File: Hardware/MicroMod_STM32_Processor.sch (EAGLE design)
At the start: 36 parts, among them J1 MICROMOD-2222, Q1 MOSFET_PCH-DMG2305UX-7, U1 STM32F405RGT6, U3 W25QXX128MBIT-6X5, Y1 12MHz, Y2 32.768kHz

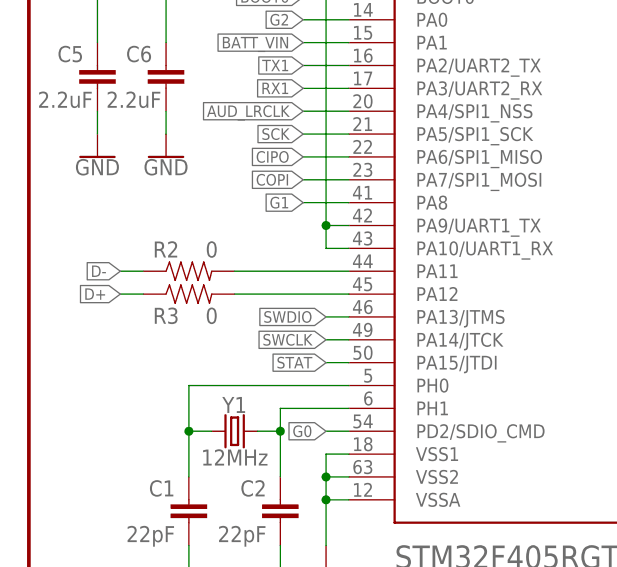
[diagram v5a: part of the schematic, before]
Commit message: Updated USB Load resistors
Replaced 0 ohm resistors with 22 ohm
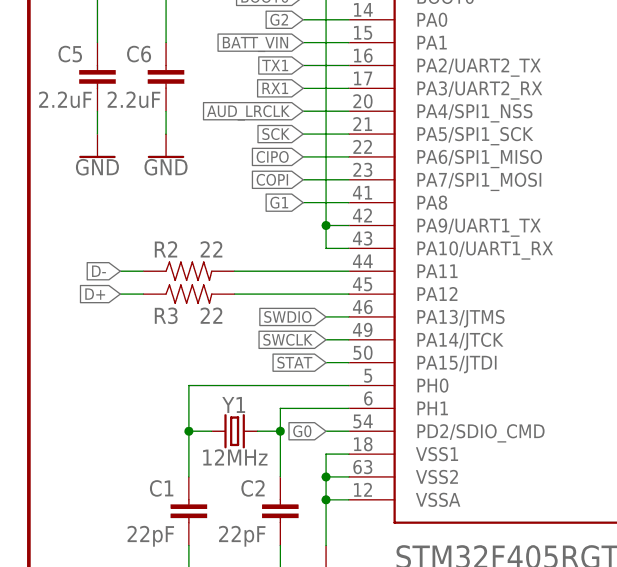
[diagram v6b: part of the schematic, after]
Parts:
- R2, R3: value 0 -> 22; device SparkFun-Resistors:0OHM-0402T-1/10W -> SparkFun-Resistors:22OHM-0402T-1/16W-1%
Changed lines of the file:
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@@
 <?xml version="1.0" encoding="utf-8"?>
 <!DOCTYPE eagle SYSTEM "eagle.dtd">
-<eagle version="9.5.2">
+<eagle version="9.6.2">
 <drawing>
 <settings>
@@
 <part name="R12" library="SparkFun-Resistors" deviceset="1KOHM" device="-0402T-1/16W-1%" value="1k"/>
 <part name="GND35" library="SparkFun-PowerSymbols" deviceset="GND" device=""/>
-<part name="R2" library="SparkFun-Resistors" deviceset="0OHM" device="-0402T-1/10W" value="0"/>
-<part name="R3" library="SparkFun-Resistors" deviceset="0OHM" device="-0402T-1/10W" value="0"/>
+<part name="R2" library="SparkFun-Resistors" deviceset="22OHM" device="-0402T-1/16W-1%" value="22"/>
+<part name="R3" library="SparkFun-Resistors" deviceset="22OHM" device="-0402T-1/16W-1%" value="22"/>
 <part name="R4" library="SparkFun-Resistors" deviceset="5.1KOHM" device="-0402T-1/16W-1%" value="5.1k"/>
 <part name="C15" library="SparkFun-Capacitors" deviceset="0.1UF" device="-0402T-10V-10%-X7R" value="0.1uF"/>

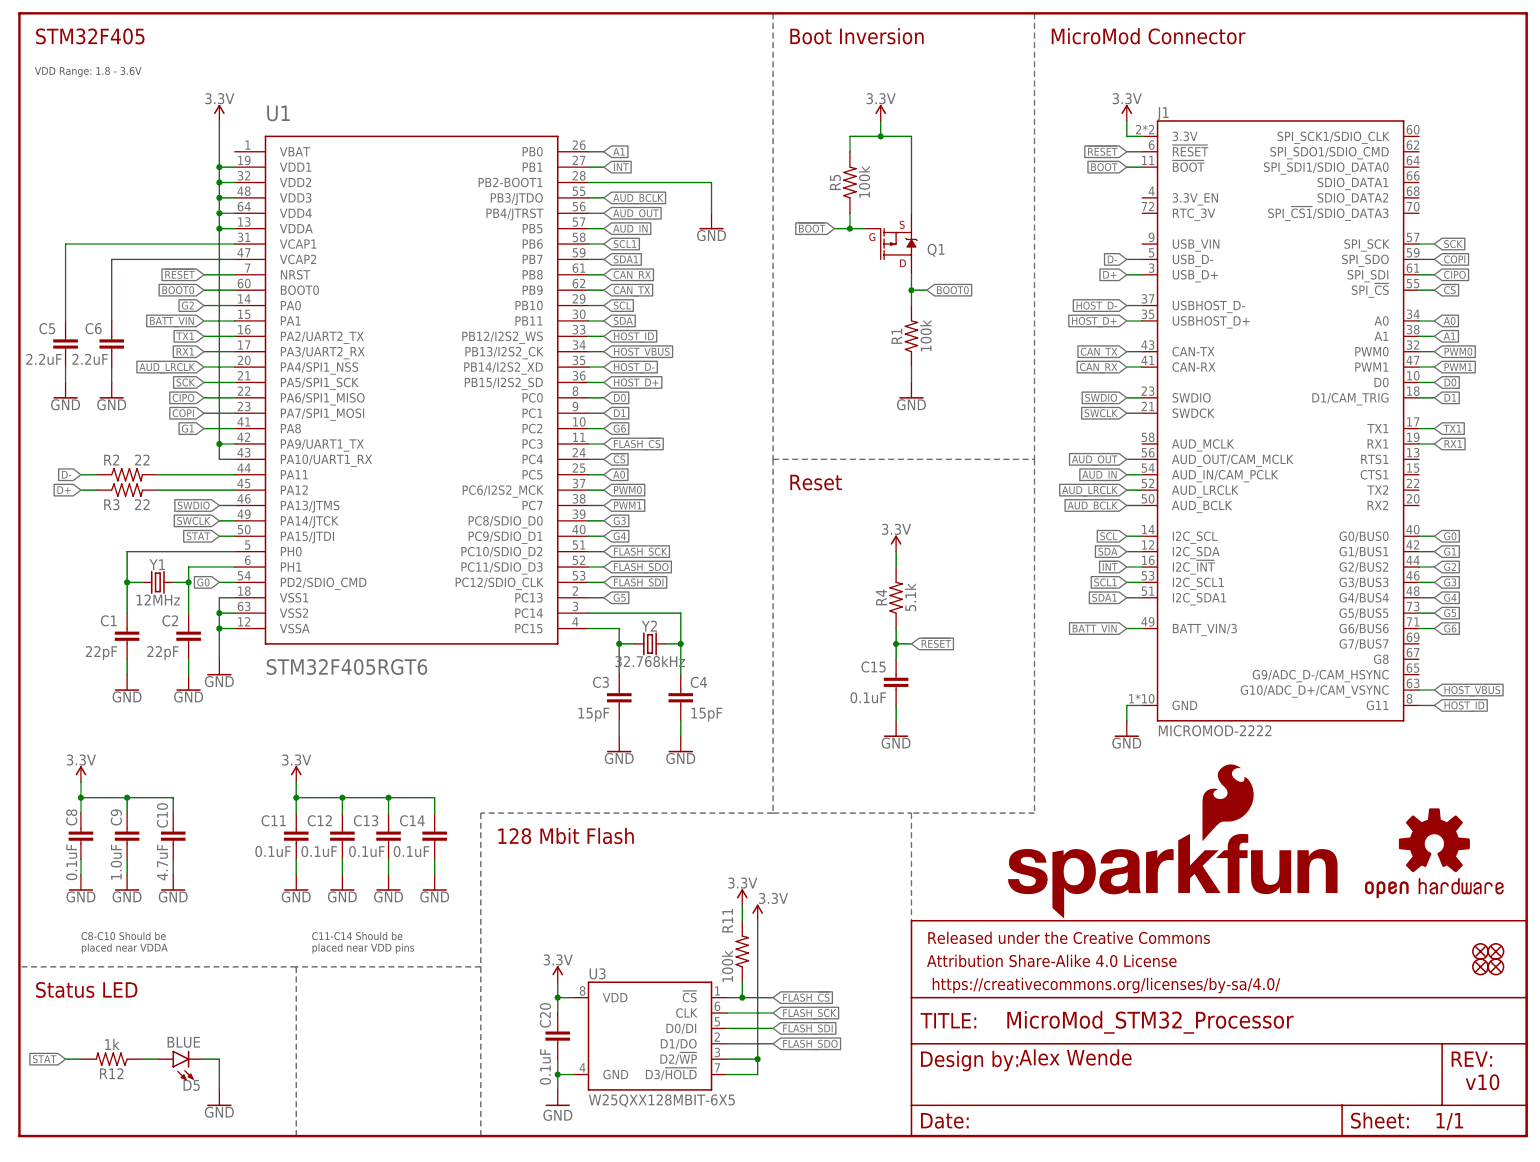
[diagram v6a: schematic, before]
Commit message: Swap USART2 for USART1, connect USART2 to ground.
Also renamed COPI/CIPO to POCI/PICO to match new naming conventions.
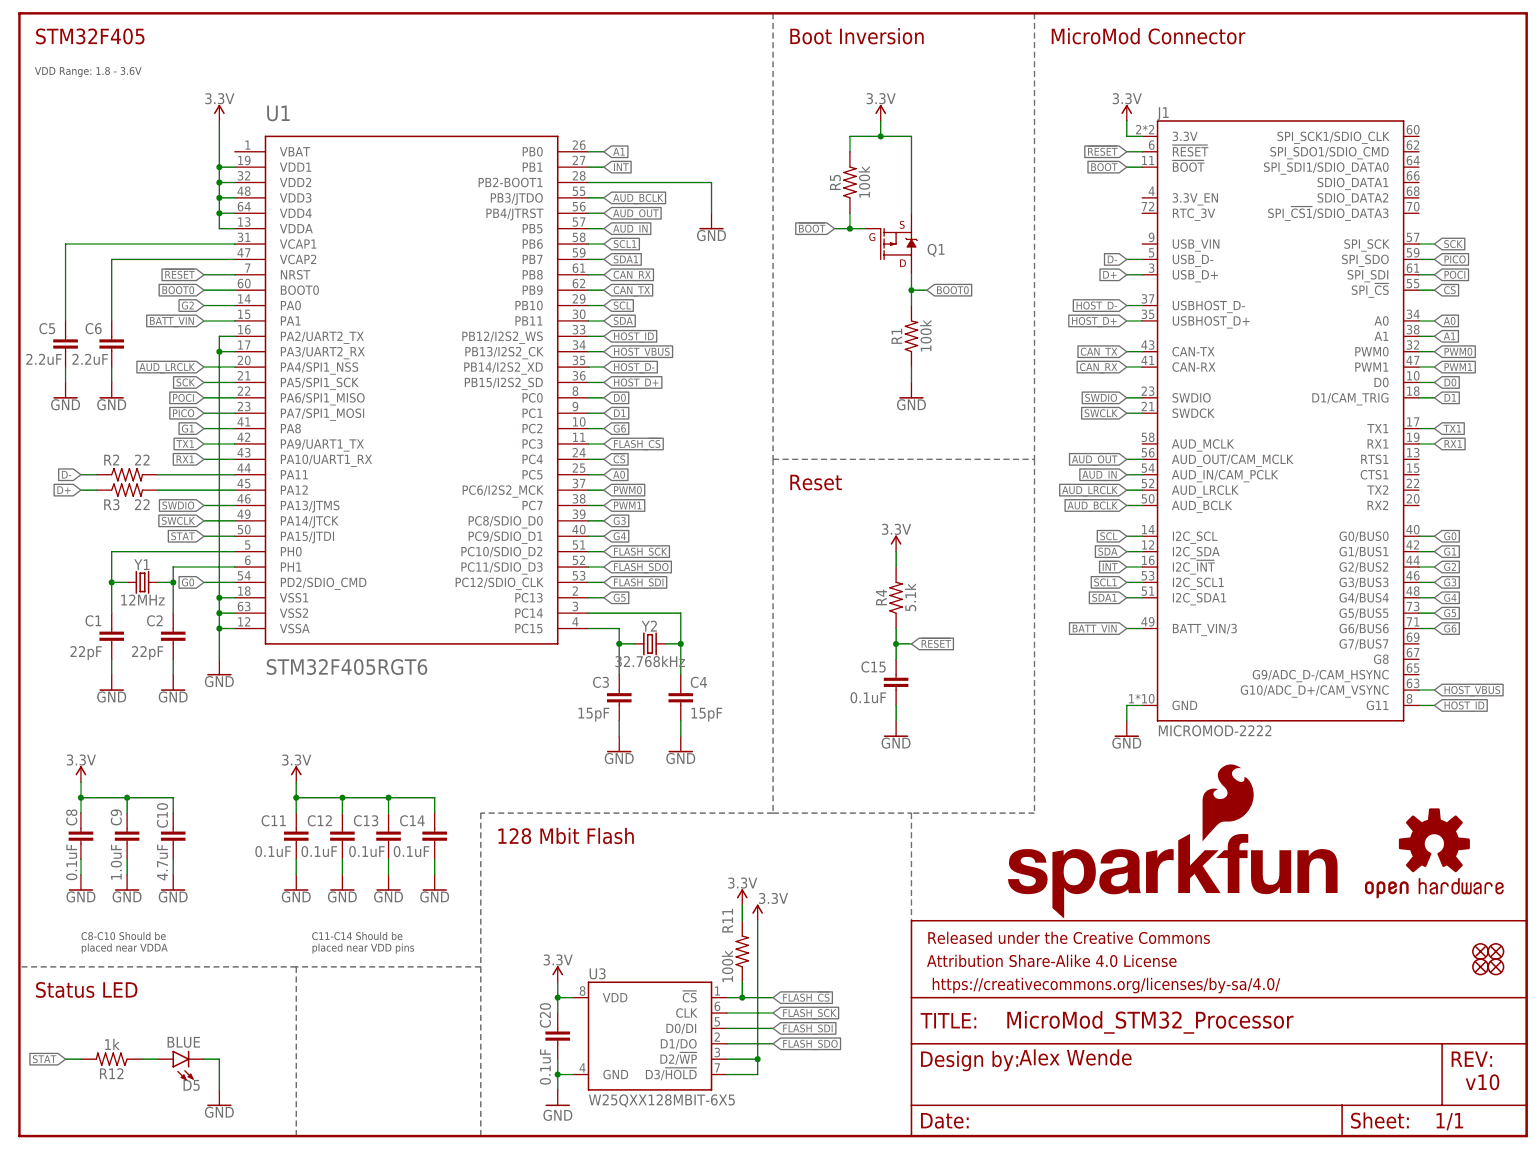
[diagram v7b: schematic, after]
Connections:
- net CIPO renamed POCI
- net COPI renamed PICO
- net 3.3V: no longer U1.PA10/UART1_RX, U1.PA9/UART1_TX
- net GND: now also U1.PA2/UART2_TX, U1.PA3/UART2_RX
- net RX1: now also U1.PA10/UART1_RX; no longer U1.PA3/UART2_RX
- net TX1: now also U1.PA9/UART1_TX; no longer U1.PA2/UART2_TX
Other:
- moved on the sheet: C1, C2, Y1
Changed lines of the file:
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@@
 <drawing>
 <settings>
-<setting alwaysvectorfont="yes"/>
+<setting alwaysvectorfont="no"/>
 <setting verticaltext="up"/>
 </settings>
@@
 <attribute name="VALUE" x="40.64" y="76.2" size="2.54" layer="96" font="vector"/>
 </instance>
-<instance part="Y1" gate="G$1" x="22.86" y="91.44" smashed="yes">
-<attribute name="NAME" x="22.86" y="93.472" size="1.778" layer="95" font="vector" align="bottom-center"/>
-<attribute name="VALUE" x="22.86" y="89.408" size="1.778" layer="96" font="vector" align="top-center"/>
+<instance part="Y1" gate="G$1" x="20.32" y="91.44" smashed="yes">
+<attribute name="NAME" x="20.32" y="93.472" size="1.778" layer="95" font="vector" align="bottom-center"/>
+<attribute name="VALUE" x="20.32" y="89.408" size="1.778" layer="96" font="vector" align="top-center"/>
 </instance>
 <instance part="Y2" gate="G$1" x="104.14" y="81.28" smashed="yes">
@@
 <attribute name="VALUE" x="104.14" y="79.248" size="1.778" layer="96" font="vector" align="top-center"/>
 </instance>
-<instance part="C1" gate="G$1" x="17.78" y="81.28" smashed="yes" rot="MR0">
-<attribute name="NAME" x="16.256" y="84.201" size="1.778" layer="95" font="vector" rot="MR0"/>
-<attribute name="VALUE" x="16.256" y="79.121" size="1.778" layer="96" font="vector" rot="MR0"/>
-</instance>
-<instance part="C2" gate="G$1" x="27.94" y="81.28" smashed="yes" rot="MR0">
-<attribute name="NAME" x="26.416" y="84.201" size="1.778" layer="95" font="vector" rot="MR0"/>
-<attribute name="VALUE" x="26.416" y="79.121" size="1.778" layer="96" font="vector" rot="MR0"/>
+<instance part="C1" gate="G$1" x="15.24" y="81.28" smashed="yes" rot="MR0">
+<attribute name="NAME" x="13.716" y="84.201" size="1.778" layer="95" font="vector" rot="MR0"/>
+<attribute name="VALUE" x="13.716" y="79.121" size="1.778" layer="96" font="vector" rot="MR0"/>
+</instance>
+<instance part="C2" gate="G$1" x="25.4" y="81.28" smashed="yes" rot="MR0">
+<attribute name="NAME" x="23.876" y="84.201" size="1.778" layer="95" font="vector" rot="MR0"/>
+<attribute name="VALUE" x="23.876" y="79.121" size="1.778" layer="96" font="vector" rot="MR0"/>
 </instance>
 <instance part="C3" gate="G$1" x="99.06" y="71.12" smashed="yes" rot="MR0">
@@
 <attribute name="VALUE" x="33.02" y="75.946" size="1.778" layer="96" font="vector" align="top-center"/>
 </instance>
-<instance part="GND6" gate="1" x="27.94" y="73.66" smashed="yes">
-<attribute name="VALUE" x="27.94" y="73.406" size="1.778" layer="96" font="vector" align="top-center"/>
-</instance>
-<instance part="GND10" gate="1" x="17.78" y="73.66" smashed="yes">
-<attribute name="VALUE" x="17.78" y="73.406" size="1.778" layer="96" font="vector" align="top-center"/>
+<instance part="GND6" gate="1" x="25.4" y="73.66" smashed="yes">
+<attribute name="VALUE" x="25.4" y="73.406" size="1.778" layer="96" font="vector" align="top-center"/>
+</instance>
+<instance part="GND10" gate="1" x="15.24" y="73.66" smashed="yes">
+<attribute name="VALUE" x="15.24" y="73.406" size="1.778" layer="96" font="vector" align="top-center"/>
 </instance>
 <instance part="GND11" gate="1" x="109.22" y="63.5" smashed="yes">
@@
 <pinref part="Y1" gate="G$1" pin="2"/>
 <pinref part="C2" gate="G$1" pin="1"/>
-<wire x1="25.4" y1="91.44" x2="27.94" y2="91.44" width="0.1524" layer="91"/>
-<wire x1="27.94" y1="91.44" x2="27.94" y2="86.36" width="0.1524" layer="91"/>
+<wire x1="22.86" y1="91.44" x2="25.4" y2="91.44" width="0.1524" layer="91"/>
+<wire x1="25.4" y1="91.44" x2="25.4" y2="86.36" width="0.1524" layer="91"/>
 <pinref part="U1" gate="G$1" pin="PH1"/>
-<wire x1="35.56" y1="93.98" x2="27.94" y2="93.98" width="0.1524" layer="91"/>
-<wire x1="27.94" y1="93.98" x2="27.94" y2="91.44" width="0.1524" layer="91"/>
-<junction x="27.94" y="91.44"/>
+<wire x1="35.56" y1="93.98" x2="25.4" y2="93.98" width="0.1524" layer="91"/>
+<wire x1="25.4" y1="93.98" x2="25.4" y2="91.44" width="0.1524" layer="91"/>
+<junction x="25.4" y="91.44"/>
 </segment>
 </net>
@@
 <pinref part="Y1" gate="G$1" pin="1"/>
 <pinref part="C1" gate="G$1" pin="1"/>
-<wire x1="20.32" y1="91.44" x2="17.78" y2="91.44" width="0.1524" layer="91"/>
-<wire x1="17.78" y1="91.44" x2="17.78" y2="86.36" width="0.1524" layer="91"/>
+<wire x1="17.78" y1="91.44" x2="15.24" y2="91.44" width="0.1524" layer="91"/>
+<wire x1="15.24" y1="91.44" x2="15.24" y2="86.36" width="0.1524" layer="91"/>
 <pinref part="U1" gate="G$1" pin="PH0"/>
-<wire x1="35.56" y1="96.52" x2="17.78" y2="96.52" width="0.1524" layer="91"/>
-<wire x1="17.78" y1="96.52" x2="17.78" y2="91.44" width="0.1524" layer="91"/>
-<junction x="17.78" y="91.44"/>
+<wire x1="35.56" y1="96.52" x2="15.24" y2="96.52" width="0.1524" layer="91"/>
+<wire x1="15.24" y1="96.52" x2="15.24" y2="91.44" width="0.1524" layer="91"/>
+<junction x="15.24" y="91.44"/>
 </segment>
 </net>
@@
 <segment>
 <pinref part="U1" gate="G$1" pin="PA13/JTMS"/>
-<wire x1="35.56" y1="104.14" x2="33.02" y2="104.14" width="0.1524" layer="91"/>
-<label x="33.02" y="104.14" size="1.27" layer="95" font="vector" rot="R180" xref="yes"/>
+<wire x1="35.56" y1="104.14" x2="30.48" y2="104.14" width="0.1524" layer="91"/>
+<label x="30.48" y="104.14" size="1.27" layer="95" font="vector" rot="R180" xref="yes"/>
 </segment>
 <segment>
@@
 <segment>
 <pinref part="U1" gate="G$1" pin="PA14/JTCK"/>
-<wire x1="35.56" y1="101.6" x2="33.02" y2="101.6" width="0.1524" layer="91"/>
-<label x="33.02" y="101.6" size="1.27" layer="95" font="vector" rot="R180" xref="yes"/>
+<wire x1="35.56" y1="101.6" x2="30.48" y2="101.6" width="0.1524" layer="91"/>
+<label x="30.48" y="101.6" size="1.27" layer="95" font="vector" rot="R180" xref="yes"/>
 </segment>
 <segment>
@@
 </segment>
 </net>
-<net name="CIPO" class="0">
+<net name="POCI" class="0">
 <segment>
 <pinref part="U1" gate="G$1" pin="PA6/SPI1_MISO"/>
@@
 </segment>
 </net>
-<net name="COPI" class="0">
+<net name="PICO" class="0">
 <segment>
 <pinref part="U1" gate="G$1" pin="PA7/SPI1_MOSI"/>
@@
 </segment>
 <segment>
-<pinref part="U1" gate="G$1" pin="PA2/UART2_TX"/>
-<wire x1="35.56" y1="132.08" x2="30.48" y2="132.08" width="0.1524" layer="91"/>
-<label x="30.48" y="132.08" size="1.27" layer="95" font="vector" rot="R180" xref="yes"/>
+<wire x1="35.56" y1="114.3" x2="30.48" y2="114.3" width="0.1524" layer="91"/>
+<label x="30.48" y="114.3" size="1.27" layer="95" font="vector" rot="R180" xref="yes"/>
+<pinref part="U1" gate="G$1" pin="PA9/UART1_TX"/>
 </segment>
 </net>
@@
 </segment>
 <segment>
-<pinref part="U1" gate="G$1" pin="PA3/UART2_RX"/>
-<wire x1="35.56" y1="129.54" x2="30.48" y2="129.54" width="0.1524" layer="91"/>
-<label x="30.48" y="129.54" size="1.27" layer="95" font="vector" rot="R180" xref="yes"/>
+<wire x1="35.56" y1="111.76" x2="30.48" y2="111.76" width="0.1524" layer="91"/>
+<label x="30.48" y="111.76" size="1.27" layer="95" font="vector" rot="R180" xref="yes"/>
+<pinref part="U1" gate="G$1" pin="PA10/UART1_RX"/>
 </segment>
 </net>
@@
 <segment>
 <pinref part="U1" gate="G$1" pin="PD2/SDIO_CMD"/>
-<wire x1="35.56" y1="91.44" x2="33.02" y2="91.44" width="0.1524" layer="91"/>
-<label x="33.02" y="91.44" size="1.27" layer="95" rot="R180" xref="yes"/>
+<wire x1="35.56" y1="91.44" x2="30.48" y2="91.44" width="0.1524" layer="91"/>
+<label x="30.48" y="91.44" size="1.27" layer="95" rot="R180" xref="yes"/>
 </segment>
 </net>
@@
 <segment>
 <pinref part="U1" gate="G$1" pin="PA15/JTDI"/>
-<wire x1="33.02" y1="99.06" x2="35.56" y2="99.06" width="0.1524" layer="91"/>
-<label x="33.02" y="99.06" size="1.27" layer="95" rot="R180" xref="yes"/>
+<wire x1="30.48" y1="99.06" x2="35.56" y2="99.06" width="0.1524" layer="91"/>
+<label x="30.48" y="99.06" size="1.27" layer="95" rot="R180" xref="yes"/>
 </segment>
 </net>
@@
 <junction x="33.02" y="83.82"/>
 <pinref part="GND4" gate="1" pin="GND"/>
+<pinref part="U1" gate="G$1" pin="PA2/UART2_TX"/>
+<wire x1="35.56" y1="132.08" x2="33.02" y2="132.08" width="0.1524" layer="91"/>
+<wire x1="33.02" y1="132.08" x2="33.02" y2="129.54" width="0.1524" layer="91"/>
+<junction x="33.02" y="88.9"/>
+<pinref part="U1" gate="G$1" pin="PA3/UART2_RX"/>
+<wire x1="33.02" y1="129.54" x2="33.02" y2="88.9" width="0.1524" layer="91"/>
+<wire x1="35.56" y1="129.54" x2="33.02" y2="129.54" width="0.1524" layer="91"/>
+<junction x="33.02" y="129.54"/>
 </segment>
 <segment>
 <pinref part="C2" gate="G$1" pin="2"/>
-<wire x1="27.94" y1="78.74" x2="27.94" y2="76.2" width="0.1524" layer="91"/>
+<wire x1="25.4" y1="78.74" x2="25.4" y2="76.2" width="0.1524" layer="91"/>
 <pinref part="GND6" gate="1" pin="GND"/>
 </segment>
 <segment>
 <pinref part="C1" gate="G$1" pin="2"/>
-<wire x1="17.78" y1="78.74" x2="17.78" y2="76.2" width="0.1524" layer="91"/>
+<wire x1="15.24" y1="78.74" x2="15.24" y2="76.2" width="0.1524" layer="91"/>
 <pinref part="GND10" gate="1" pin="GND"/>
 </segment>
@@
 </segment>
 <segment>
-<pinref part="U1" gate="G$1" pin="PA10/UART1_RX"/>
-<wire x1="35.56" y1="111.76" x2="33.02" y2="111.76" width="0.1524" layer="91"/>
-<wire x1="33.02" y1="111.76" x2="33.02" y2="114.3" width="0.1524" layer="91"/>
-<pinref part="U1" gate="G$1" pin="PA9/UART1_TX"/>
-<wire x1="33.02" y1="114.3" x2="33.02" y2="149.86" width="0.1524" layer="91"/>
 <wire x1="33.02" y1="149.86" x2="33.02" y2="152.4" width="0.1524" layer="91"/>
 <wire x1="33.02" y1="152.4" x2="33.02" y2="154.94" width="0.1524" layer="91"/>
@@
 <wire x1="33.02" y1="157.48" x2="33.02" y2="160.02" width="0.1524" layer="91"/>
 <wire x1="33.02" y1="160.02" x2="33.02" y2="167.64" width="0.1524" layer="91"/>
-<wire x1="35.56" y1="114.3" x2="33.02" y2="114.3" width="0.1524" layer="91"/>
-<junction x="33.02" y="114.3"/>
 <pinref part="U1" gate="G$1" pin="VDDA"/>
 <wire x1="35.56" y1="149.86" x2="33.02" y2="149.86" width="0.1524" layer="91"/>
-<junction x="33.02" y="149.86"/>
 <pinref part="U1" gate="G$1" pin="VDD4"/>
 <wire x1="35.56" y1="152.4" x2="33.02" y2="152.4" width="0.1524" layer="91"/>
